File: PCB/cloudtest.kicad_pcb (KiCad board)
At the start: 2 copper layers, 47 x 36.5 mm, 10 parts, among them J1 PulseIn, J2 Display, U1 ESP32-C3_SUPERMINI_TH, U2 MIC5219-5.0YM5, U3 MIC5219-3.3YM5

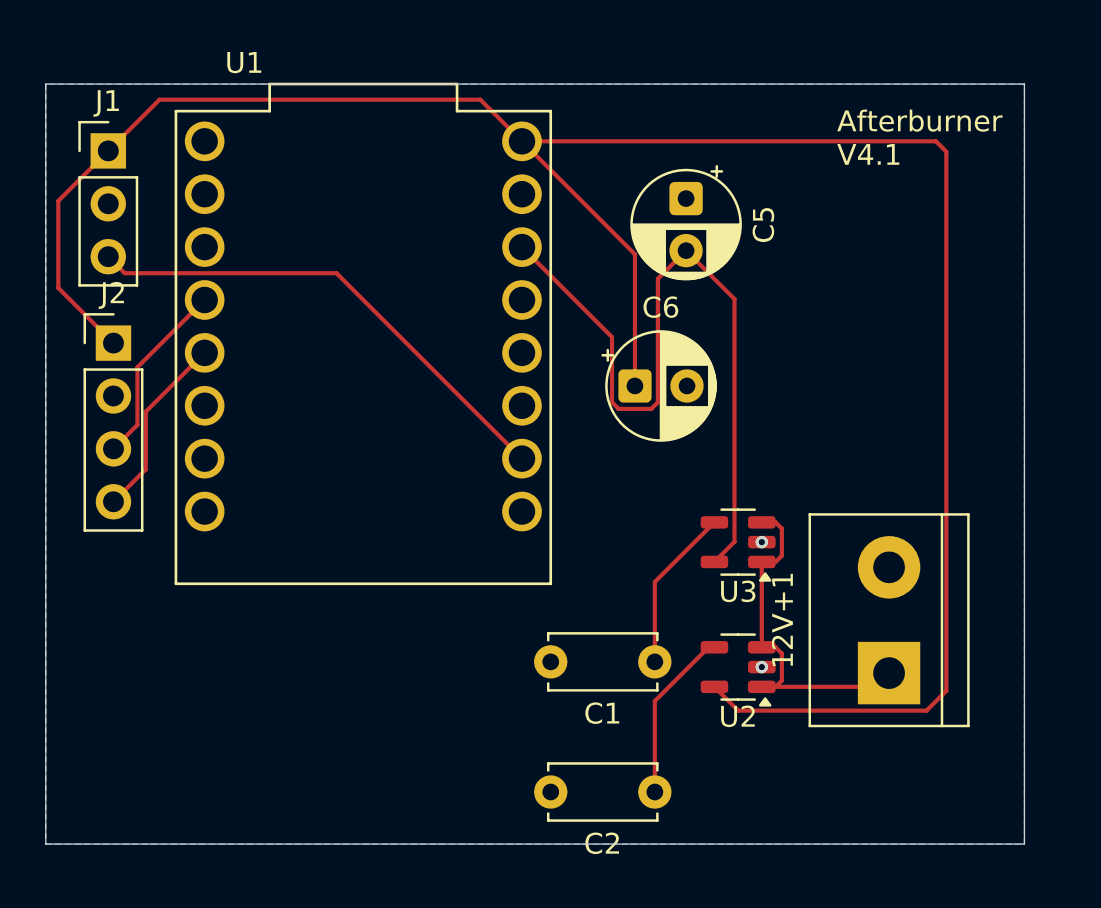
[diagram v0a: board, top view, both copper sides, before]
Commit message: PCB update, remove power delivery
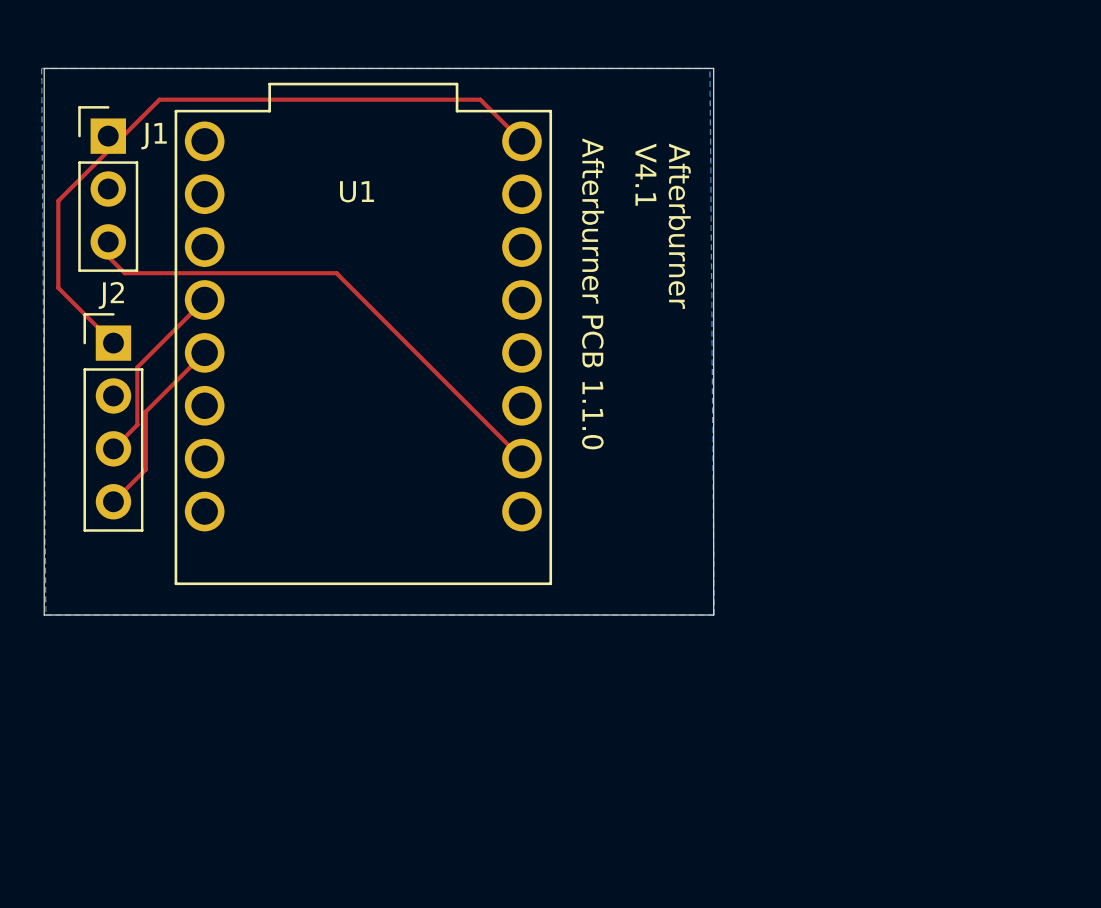
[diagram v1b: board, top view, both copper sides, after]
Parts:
- removed 12V+1: Screw_Terminal_01x02, TerminalBlock:TerminalBlock_bornier-2_P5.08mm
- removed C1, C2: 470pf, Capacitor_THT:C_Disc_D5.0mm_W2.5mm_P5.00mm
- removed C5, C6: 2.2uf, Capacitor_THT:CP_Radial_D5.0mm_P2.50mm
- removed U2: MIC5219-5.0YM5, Package_TO_SOT_SMD:SOT-23-5
- removed U3: MIC5219-3.3YM5, Package_TO_SOT_SMD:SOT-23-5
- moved J1 0.71 mm to (23.5, 64.5)
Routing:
- net VCC: track 105.7 -> 33.0 mm
- net +3.3V: track 35.9 -> 0.00 mm
- net +12V: track 17.4 -> 0.00 mm
- net Net-(U2-BP): track 8.30 -> 0.00 mm
- net Net-(U3-BP): track 7.89 -> 0.00 mm
- net GND: vias 2 -> 0
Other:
- board size 47 x 36.5 mm -> 32.2 x 26.2 mm
- board text added: "Afterburner PCB 1.1.0"

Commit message: PCB update
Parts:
- J1: footprint Connector_PinHeader_2.54mm:PinHeader_1x03_P2.54mm_Vertical -> Library:PinHeader_1x03_P2.54mm_Vertical
- J2: footprint Connector_PinHeader_2.54mm:PinHeader_1x04_P2.54mm_Vertical -> Library:PinHeader_1x04_P2.54mm_Vertical
- U1: footprint ESP32-C3_SUPERMINI_TH(2):MODULE_ESP32-C3_SUPERMINI -> Library:MODULE_ESP32-C3_SUPERMINI
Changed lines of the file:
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@@
 	(net 15 "/i2c esp sda")
 	(net 16 "VCC")
-	(footprint "Connector_PinHeader_2.54mm:PinHeader_1x04_P2.54mm_Vertical"
+	(footprint "Library:PinHeader_1x04_P2.54mm_Vertical"
 		(layer "F.Cu")
 		(at 23.75 74.44)
@@
 		)
 	)
-	(footprint "Connector_PinHeader_2.54mm:PinHeader_1x03_P2.54mm_Vertical"
+	(footprint "Library:PinHeader_1x03_P2.54mm_Vertical"
 		(layer "F.Cu")
 		(at 23.5 64.5)
@@
 		)
 	)
-	(footprint "ESP32-C3_SUPERMINI_TH(2):MODULE_ESP32-C3_SUPERMINI"
+	(footprint "Library:MODULE_ESP32-C3_SUPERMINI"
 		(layer "F.Cu")
 		(at 35.75 74.65)

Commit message: updated readme
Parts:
- moved J1 0.30 mm to (23.8, 64.5)
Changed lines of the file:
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@@
 		(tenting front back)
 		(pcbplotparams
-			(layerselection 0x00000000_00000000_55555555_5755f5ff)
+			(layerselection 0x00000000_00000000_55557fd5_57fff5ff)
 			(plot_on_all_layers_selection 0x00000000_00000000_00000000_00000000)
 			(disableapertmacros no)
@@
 		(tags "Through hole pin header THT 1x04 2.54mm single row")
 		(property "Reference" "J2"
-			(at 0 -2.38 0)
+			(at -2.05 -0.09 0)
 			(layer "F.SilkS")
 			(effects
@@
 	(footprint "Library:PinHeader_1x03_P2.54mm_Vertical"
 		(layer "F.Cu")
-		(at 23.5 64.5)
+		(at 23.8 64.47)
 		(descr "Through hole straight pin header, 1x03, 2.54mm pitch, single row")
 		(tags "Through hole pin header THT 1x03 2.54mm single row")
 		(property "Reference" "J1"
-			(at 2.3 -0.1 0)
-			(layer "F.SilkS")
-			(effects
+			(at -2 0.38 0)
+			(layer "F.SilkS")
+			(effects
